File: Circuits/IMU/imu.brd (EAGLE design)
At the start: 16.4 x 12.2 mm, 11 parts, among them U1 LSM9DS1

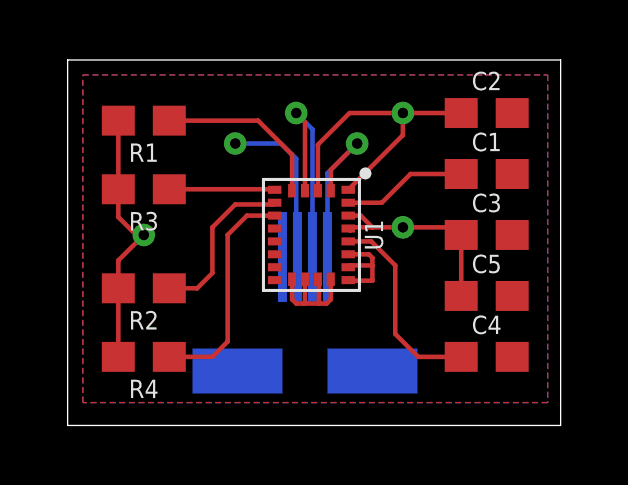
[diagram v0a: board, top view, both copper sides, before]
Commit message: Update board/schematic/custom library with 1 mm pitch connector
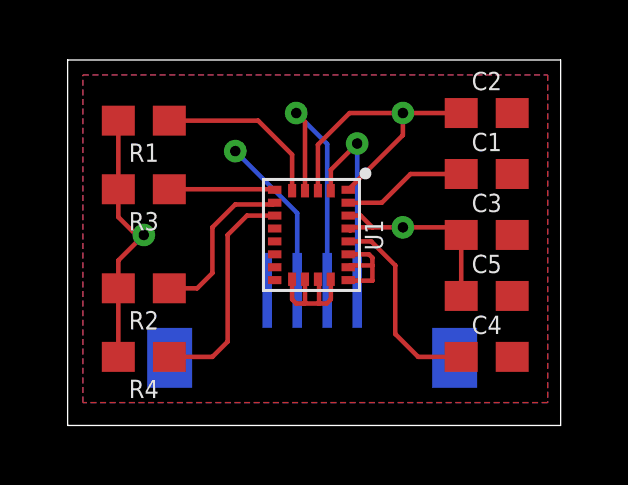
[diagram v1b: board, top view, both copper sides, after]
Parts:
- U$1: value MOLEX_5034800400 -> MOLEX_522070433; device custom:MOLEX4 -> custom:MOLEX4_1MM
- moved U$1 1.28 mm to (49.0, 32.0)
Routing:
- net SDA: track 7.73 -> 9.05 mm
- net SCL: track 6.13 -> 6.83 mm
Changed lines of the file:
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@@
 <attribute name="VALUE" x="45.72" y="35.052" size="0.6096" layer="27" font="vector" ratio="20" rot="R270" align="top-center"/>
 </element>
-<element name="U$1" library="custom" package="MOLEX4" value="MOLEX_5034800400" x="48.0314" y="32.8168" smashed="yes" rot="MR0"/>
+<element name="U$1" library="custom" package="MOLEX4_1MM" value="MOLEX_522070433" x="49.022" y="32.004" smashed="yes" rot="MR0">
+<attribute name="NAME" x="56.722" y="32.804" size="1.27" layer="26" rot="MR0"/>
+<attribute name="VALUE" x="56.822" y="28.204" size="1.27" layer="26" rot="MR0"/>
+</element>
 </elements>
 <signals>
@@
 <vertex x="39.878" y="29.464"/>
 </polygon>
-<contactref element="U$1" pad="3"/>
-<wire x1="47.0314" y1="34.3168" x2="46.99" y2="34.3582" width="0.1524" layer="16"/>
-<wire x1="46.99" y1="34.3582" x2="46.99" y2="37.592" width="0.1524" layer="16"/>
-<wire x1="46.99" y1="37.592" x2="46.482" y2="38.1" width="0.1524" layer="16"/>
-<wire x1="46.482" y1="38.1" x2="44.958" y2="38.1" width="0.1524" layer="16"/>
-<via x="44.958" y="38.1" extent="1-16" drill="0.35"/>
 <wire x1="46.853" y1="33.577" x2="46.853" y2="32.903" width="0.1524" layer="1"/>
 <wire x1="46.853" y1="32.903" x2="46.99" y2="32.766" width="0.1524" layer="1"/>
@@
 <wire x1="48.723" y1="33.977" x2="48.782" y2="34.036" width="0.1524" layer="1"/>
 <wire x1="48.782" y1="34.036" x2="49.53" y2="34.036" width="0.1524" layer="1"/>
+<contactref element="U$1" pad="3"/>
+<wire x1="47.022" y1="33.204" x2="47.022" y2="35.782" width="0.1524" layer="16"/>
+<wire x1="47.022" y1="35.782" x2="44.958" y2="37.846" width="0.1524" layer="16"/>
+<via x="44.958" y="37.846" extent="1-16" drill="0.35"/>
 </signal>
 <signal name="C1">
@@
 <vertex x="39.878" y="29.464"/>
 </polygon>
-<contactref element="U$1" pad="4"/>
 <wire x1="52.49" y1="39.116" x2="50.546" y2="39.116" width="0.1524" layer="1"/>
 <via x="50.546" y="39.116" extent="1-16" drill="0.35"/>
@@
 <wire x1="47.713" y1="38.061" x2="48.768" y2="39.116" width="0.1524" layer="1"/>
 <wire x1="48.768" y1="39.116" x2="50.546" y2="39.116" width="0.1524" layer="1"/>
+<contactref element="U$1" pad="4"/>
 </signal>
 <signal name="SA0">
@@
 <signal name="SDA">
 <contactref element="U1" pad="4"/>
-<contactref element="U$1" pad="2"/>
-<wire x1="47.5314" y1="34.3168" x2="47.5314" y2="38.5746" width="0.1524" layer="16"/>
-<wire x1="47.5314" y1="38.5746" x2="46.99" y2="39.116" width="0.1524" layer="16"/>
 <via x="46.99" y="39.116" extent="1-16" drill="0.35"/>
 <wire x1="47.283" y1="36.527" x2="47.283" y2="38.823" width="0.1524" layer="1"/>
 <wire x1="47.283" y1="38.823" x2="46.99" y2="39.116" width="0.1524" layer="1"/>
+<contactref element="U$1" pad="2"/>
+<wire x1="48.022" y1="33.204" x2="48.022" y2="38.084" width="0.1524" layer="16"/>
+<wire x1="48.022" y1="38.084" x2="46.99" y2="39.116" width="0.1524" layer="16"/>
 </signal>
 <signal name="SCL">
 <contactref element="U1" pad="2"/>
-<contactref element="U$1" pad="1"/>
-<wire x1="48.0314" y1="34.3168" x2="48.0314" y2="37.1094" width="0.1524" layer="16"/>
-<wire x1="48.0314" y1="37.1094" x2="49.022" y2="38.1" width="0.1524" layer="16"/>
 <via x="49.022" y="38.1" extent="1-16" drill="0.35"/>
 <wire x1="48.143" y1="36.527" x2="48.143" y2="37.221" width="0.1524" layer="1"/>
 <wire x1="48.143" y1="37.221" x2="49.022" y2="38.1" width="0.1524" layer="1"/>
+<contactref element="U$1" pad="1"/>
+<wire x1="49.022" y1="33.204" x2="49.022" y2="38.1" width="0.1524" layer="16"/>
 </signal>
 </signals>

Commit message: Remove connector silkscreen
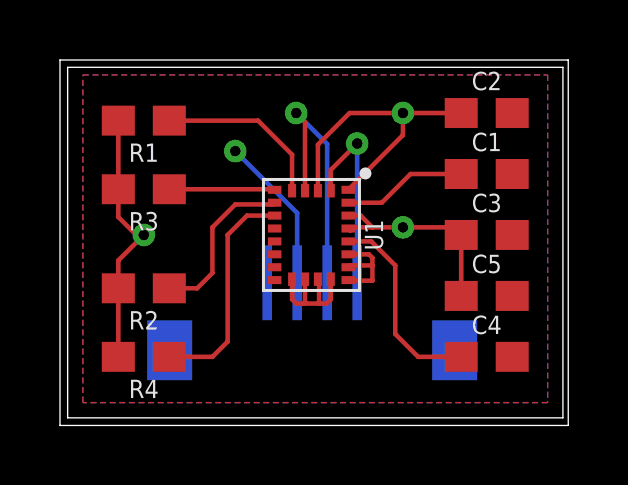
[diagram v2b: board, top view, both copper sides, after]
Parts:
- moved U$1 0.25 mm to (49.0, 32.3)
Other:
- board size 16.4 x 12.2 mm -> 16.9 x 12.2 mm
- board text added: "conn"
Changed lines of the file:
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@@
 <drawing>
 <settings>
-<setting alwaysvectorfont="no"/>
+<setting alwaysvectorfont="yes"/>
 <setting verticaltext="up"/>
 </settings>
@@
 <board>
 <plain>
-<wire x1="39.37" y1="28.702" x2="55.804" y2="28.702" width="0" layer="20"/>
-<wire x1="55.804" y1="28.702" x2="55.804" y2="40.884" width="0" layer="20"/>
-<wire x1="55.804" y1="40.884" x2="39.37" y2="40.884" width="0" layer="20"/>
-<wire x1="39.37" y1="40.884" x2="39.37" y2="28.702" width="0" layer="20"/>
+<wire x1="39.116" y1="28.702" x2="56.058" y2="28.702" width="0" layer="20"/>
+<wire x1="56.058" y1="28.702" x2="56.058" y2="40.884" width="0" layer="20"/>
+<wire x1="56.058" y1="40.884" x2="39.116" y2="40.884" width="0" layer="20"/>
+<wire x1="39.116" y1="40.884" x2="39.116" y2="28.702" width="0" layer="20"/>
+<wire x1="39.37" y1="40.64" x2="55.88" y2="40.64" width="0" layer="20"/>
+<wire x1="55.88" y1="40.64" x2="55.88" y2="28.956" width="0" layer="20"/>
+<wire x1="55.88" y1="28.956" x2="39.37" y2="28.956" width="0" layer="20"/>
+<wire x1="39.37" y1="28.956" x2="39.37" y2="40.64" width="0" layer="20"/>
+<text x="48.26" y="30.734" size="0.6096" layer="22" rot="MR0">conn</text>
 </plain>
 <attributes>
@@
 <attribute name="VALUE" x="45.72" y="35.052" size="0.6096" layer="27" font="vector" ratio="20" rot="R270" align="top-center"/>
 </element>
-<element name="U$1" library="custom" package="MOLEX4_1MM" value="MOLEX_522070433" x="49.022" y="32.004" smashed="yes" rot="MR0">
-<attribute name="NAME" x="56.722" y="32.804" size="1.27" layer="26" rot="MR0"/>
-<attribute name="VALUE" x="56.822" y="28.204" size="1.27" layer="26" rot="MR0"/>
-</element>
+<element name="U$1" library="custom" package="MOLEX4_1MM" value="MOLEX_522070433" x="49.022" y="32.258" smashed="yes" rot="MR0"/>
 </elements>
 <signals>
@@
 <wire x1="48.782" y1="34.036" x2="49.53" y2="34.036" width="0.1524" layer="1"/>
 <contactref element="U$1" pad="3"/>
-<wire x1="47.022" y1="33.204" x2="47.022" y2="35.782" width="0.1524" layer="16"/>
+<wire x1="47.022" y1="33.458" x2="47.022" y2="35.782" width="0.1524" layer="16"/>
 <wire x1="47.022" y1="35.782" x2="44.958" y2="37.846" width="0.1524" layer="16"/>
 <via x="44.958" y="37.846" extent="1-16" drill="0.35"/>
@@
 <wire x1="47.283" y1="36.527" x2="47.283" y2="38.823" width="0.1524" layer="1"/>
 <wire x1="47.283" y1="38.823" x2="46.99" y2="39.116" width="0.1524" layer="1"/>
+<wire x1="48.022" y1="38.084" x2="46.99" y2="39.116" width="0.1524" layer="16"/>
 <contactref element="U$1" pad="2"/>
-<wire x1="48.022" y1="33.204" x2="48.022" y2="38.084" width="0.1524" layer="16"/>
-<wire x1="48.022" y1="38.084" x2="46.99" y2="39.116" width="0.1524" layer="16"/>
+<wire x1="48.022" y1="33.458" x2="48.022" y2="38.084" width="0.1524" layer="16"/>
 </signal>
 <signal name="SCL">
@@
 <wire x1="48.143" y1="37.221" x2="49.022" y2="38.1" width="0.1524" layer="1"/>
 <contactref element="U$1" pad="1"/>
-<wire x1="49.022" y1="33.204" x2="49.022" y2="38.1" width="0.1524" layer="16"/>
+<wire x1="49.022" y1="33.458" x2="49.022" y2="38.1" width="0.1524" layer="16"/>
 </signal>
 </signals>

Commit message: Remove silkscreen outline
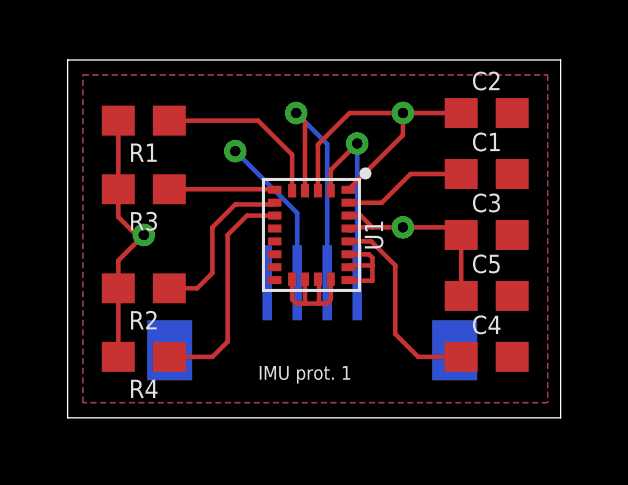
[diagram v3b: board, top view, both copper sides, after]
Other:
- board size 16.9 x 12.2 mm -> 16.4 x 11.9 mm
- board text added: "IMU prot. 1"
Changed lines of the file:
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@@
 <board>
 <plain>
-<wire x1="39.116" y1="28.702" x2="56.058" y2="28.702" width="0" layer="20"/>
-<wire x1="56.058" y1="28.702" x2="56.058" y2="40.884" width="0" layer="20"/>
-<wire x1="56.058" y1="40.884" x2="39.116" y2="40.884" width="0" layer="20"/>
-<wire x1="39.116" y1="40.884" x2="39.116" y2="28.702" width="0" layer="20"/>
-<wire x1="39.37" y1="40.64" x2="55.88" y2="40.64" width="0" layer="20"/>
-<wire x1="55.88" y1="40.64" x2="55.88" y2="28.956" width="0" layer="20"/>
-<wire x1="55.88" y1="28.956" x2="39.37" y2="28.956" width="0" layer="20"/>
-<wire x1="39.37" y1="28.956" x2="39.37" y2="40.64" width="0" layer="20"/>
+<wire x1="39.37" y1="28.956" x2="55.804" y2="28.956" width="0" layer="20"/>
+<wire x1="55.804" y1="28.956" x2="55.804" y2="40.884" width="0" layer="20"/>
+<wire x1="55.804" y1="40.884" x2="39.37" y2="40.884" width="0" layer="20"/>
+<wire x1="39.37" y1="40.884" x2="39.37" y2="28.956" width="0" layer="20"/>
 <text x="48.26" y="30.734" size="0.6096" layer="22" rot="MR0">conn</text>
+<text x="45.72" y="30.226" size="0.4572" layer="21">IMU prot. 1</text>
 </plain>
 <attributes>
